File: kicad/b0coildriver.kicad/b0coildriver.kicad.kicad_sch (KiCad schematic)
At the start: 42 parts, among them J1 Vctrl, J2 PSU, J3 COIL, J4 Screw_Terminal_01x04, J5 ISense, U1 LM358, U2 OPA549T, U3 74HC04, U4 CMS2005

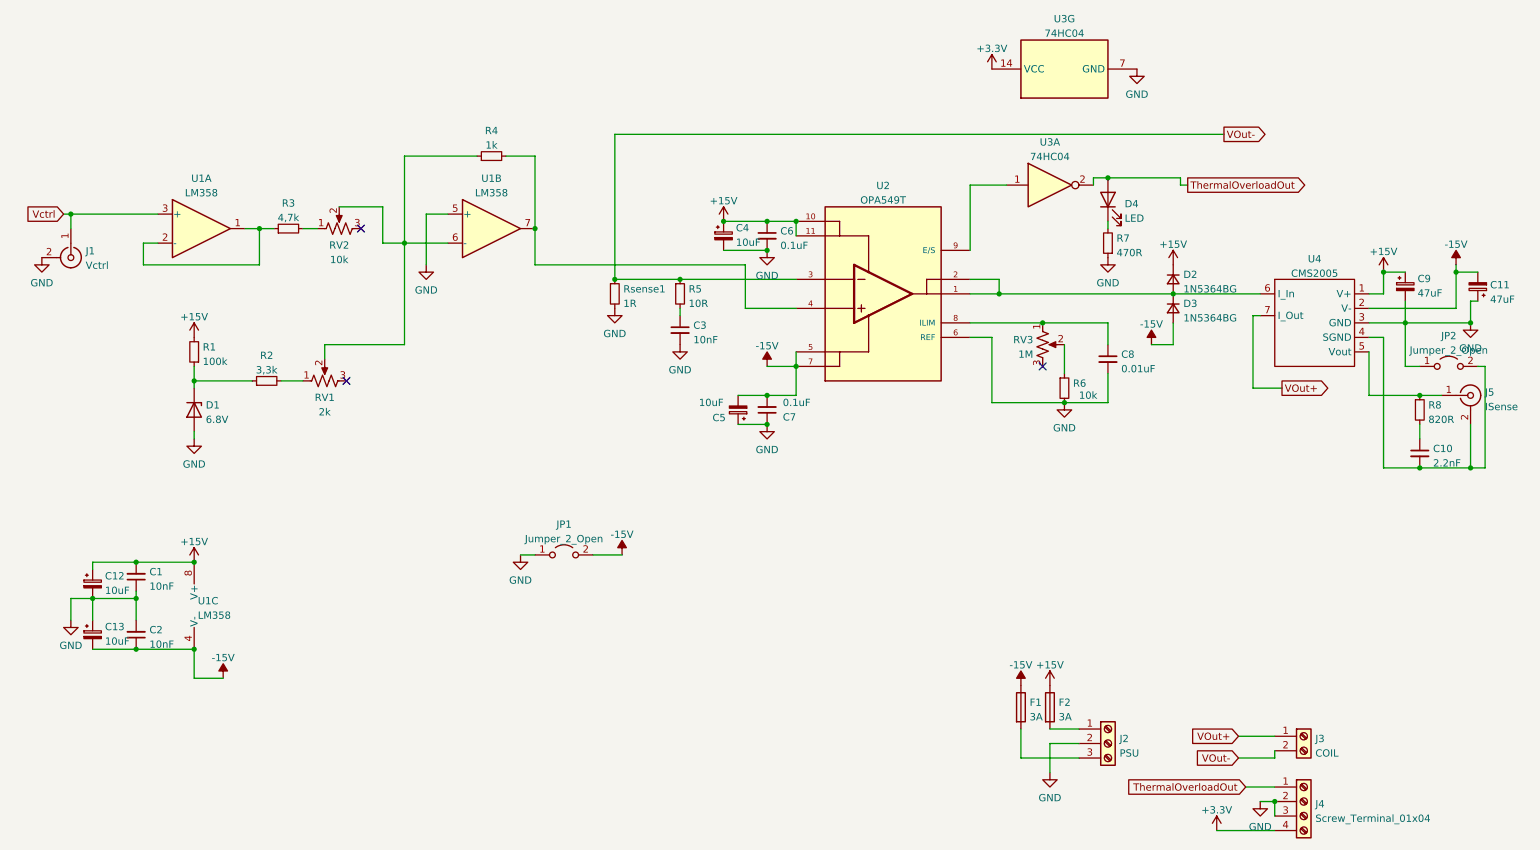
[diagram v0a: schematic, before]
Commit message: Temperature compensating feedback network
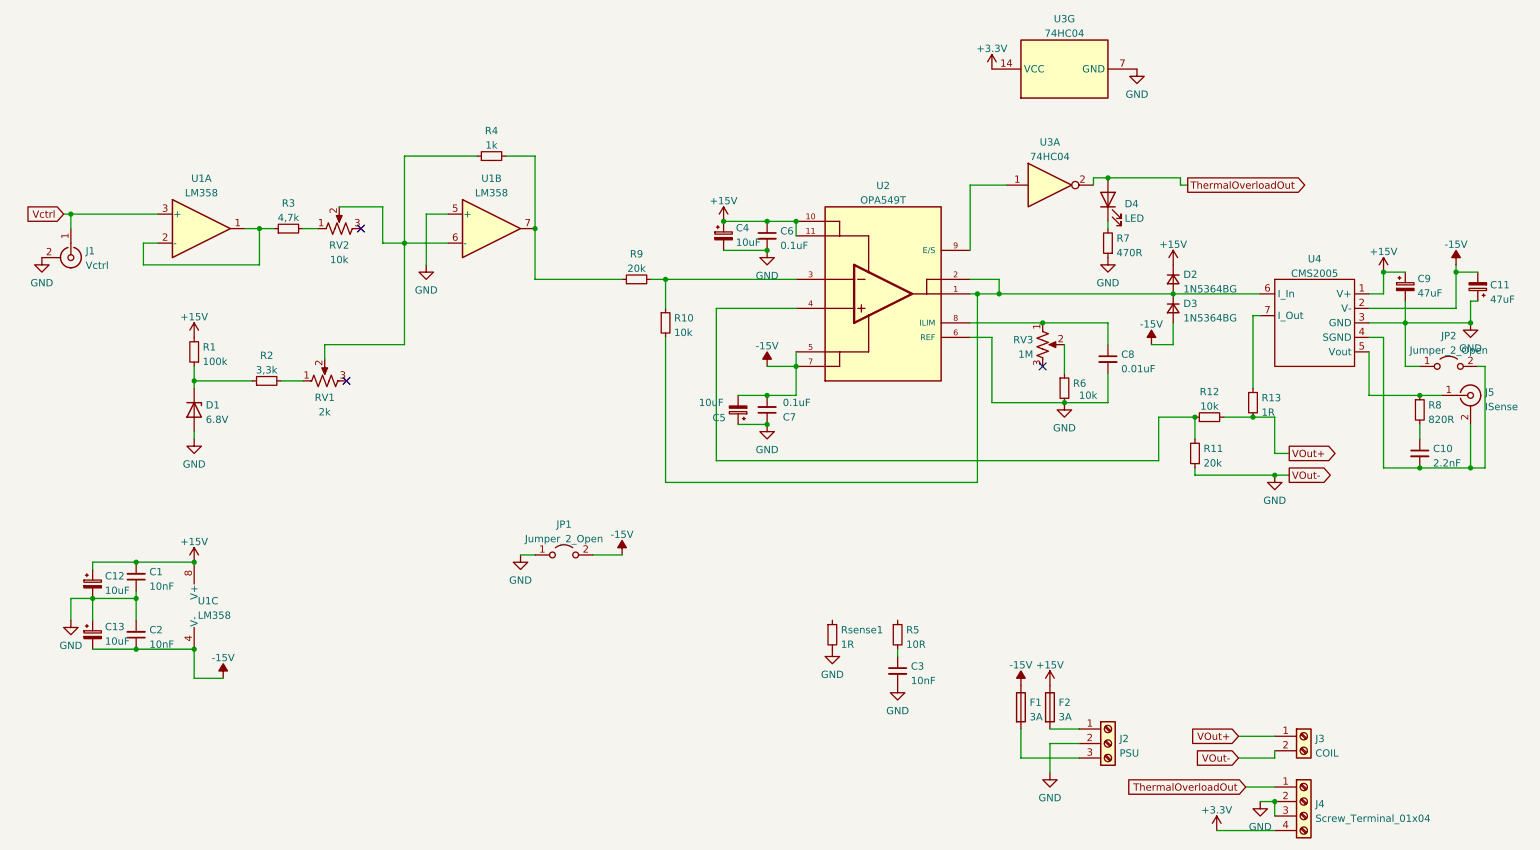
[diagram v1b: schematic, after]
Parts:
- added R10, R12: 10k, symbol Device:R_Small
- added R11, R9: 20k, symbol Device:R_Small
- added R13: 1R, symbol Device:R_Small
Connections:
- net GND: now also J3.2 (Pin_2), R11.1
- net VOut+: now also R12.2, R13.2; no longer U4.7 (I_Out)
- net at D2.2 (A), D3.1 (K), U2.1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: now also R10.2
- net at R4.2, U1.7: now also R9.1; no longer U2.4
- removed net VOut-: J3.2 (Pin_2), R5.1, Rsense1.1, U2.3
- new net: R11.2, R12.1, U2.4
- new net: R10.1, R9.2, U2.3
- new net: R13.1, U4.7 (I_Out)
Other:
- moved on the sheet: C3, R5, Rsense1

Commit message: Updated board layout to new feedback network
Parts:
- removed C3: 10nF, Capacitor_THT:C_Rect_L7.0mm_W2.0mm_P5.00mm, symbol Device:C_Small
- removed R5: 10R, Resistor_THT:R_Axial_DIN0207_L6.3mm_D2.5mm_P10.16mm_Horizontal, symbol Device:R_Small
- removed Rsense1: 1R, Connector_PinSocket_2.54mm:PinSocket_1x02_P2.54mm_Vertical, symbol Device:R_Small
- R10, R11, R12, R13, R9: footprint (none) -> Resistor_THT:R_Axial_DIN0207_L6.3mm_D2.5mm_P10.16mm_Horizontal
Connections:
- net at C8.1, RV3.1, U2.8 (ILIM): now also RV3.2
- net at R4.1, RV1.2, RV2.2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: now also RV1.3, RV2.3
- net at R6.1: now also RV3.3; no longer RV3.2
- no-connect marks 3 -> 0

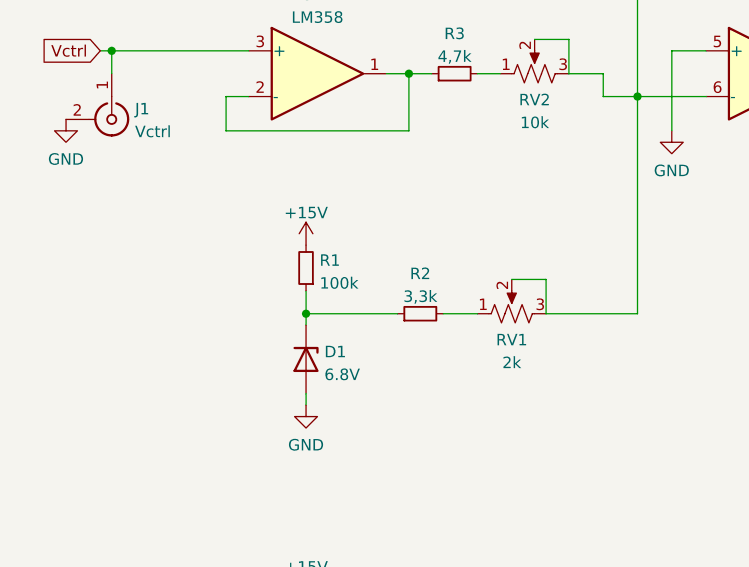
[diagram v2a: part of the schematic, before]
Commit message: Fixed value of pullup at voltage reference
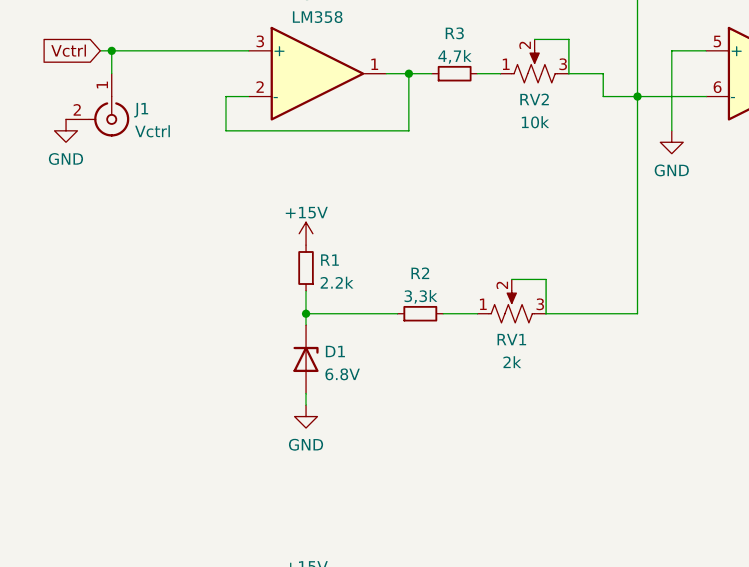
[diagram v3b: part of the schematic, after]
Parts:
- R1: value 100k -> 2.2k
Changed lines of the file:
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@@
       (effects (font (size 1.27 1.27)) (justify right))
     )
-    (property "Value" "100k" (id 1) (at 58.6486 79.1722 0)
+    (property "Value" "2.2k" (id 1) (at 58.6486 79.1722 0)
       (effects (font (size 1.27 1.27)) (justify right))
     )
@@
     )
     (path "/ecd6e557-6424-43b3-bb05-b304d5281e8c"
-      (reference "R1") (unit 1) (value "100k") (footprint "Resistor_THT:R_Axial_DIN0207_L6.3mm_D2.5mm_P10.16mm_Horizontal")
+      (reference "R1") (unit 1) (value "2.2k") (footprint "Resistor_THT:R_Axial_DIN0207_L6.3mm_D2.5mm_P10.16mm_Horizontal")
     )
     (path "/6778cc9c-40aa-49e6-b579-e7041a776a97"
